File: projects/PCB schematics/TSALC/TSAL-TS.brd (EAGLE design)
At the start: 81.3 x 95.2 mm, 29 parts, among them J1 2P_1-770166-0, J2 2P_1-770166-0, J3 2P_1-770166-0, J4 2P_1-770166-0, X2 5566-2, X3 5566-2

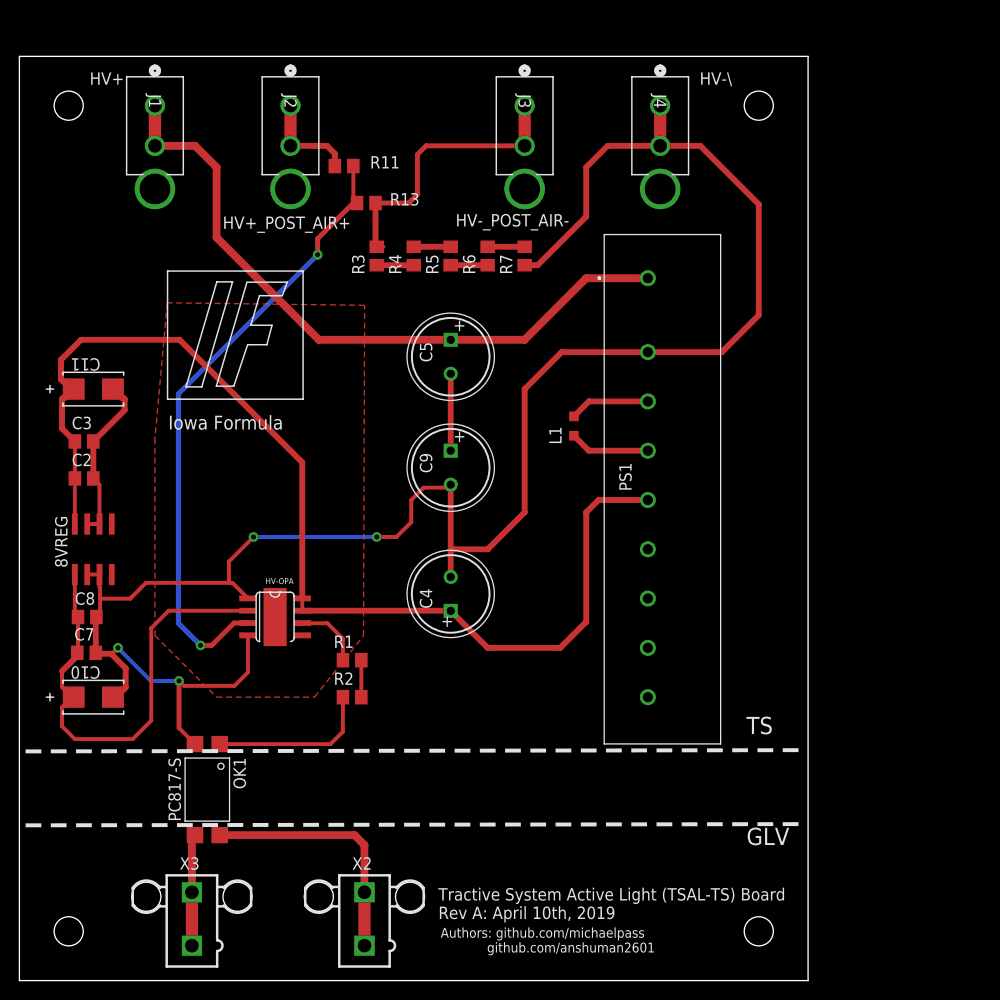
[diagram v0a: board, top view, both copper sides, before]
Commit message: TSALC - TS; Rev A.
Adding in silkscreen markings.
Board has TS and GLV markings separated by 8.26mm. This is the limit imposed by the optocoupler. The rules state that optocouplers are exempt. However, they will likely consider any copper leading up to the device to be TS components to be dealt with.

TSALC - TS; Rev A. Pull request #5.

TSALC boards now ready for pull request review.

---SQUASH---

TSALC - Capacitors updated with new EDA files.

Capacitors now current.
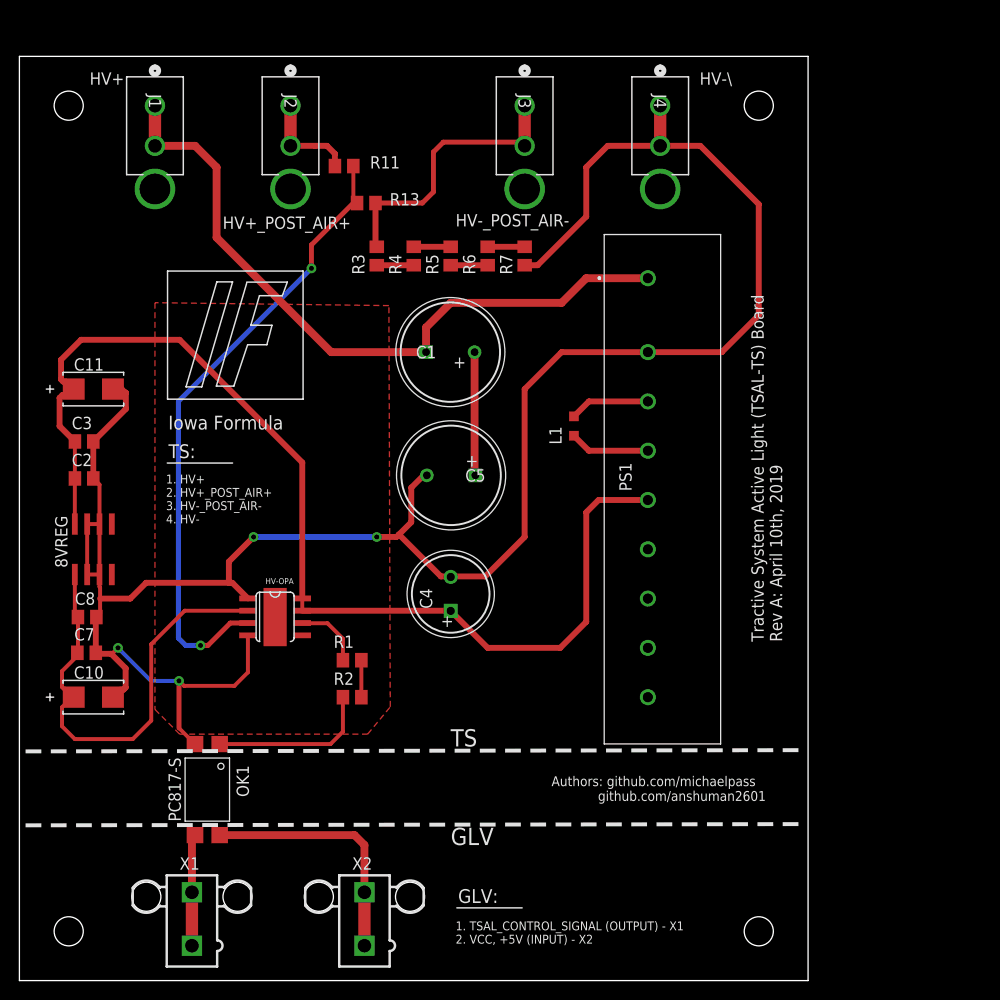
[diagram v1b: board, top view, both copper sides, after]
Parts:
- removed C9: EEU-FS1H221L, EEU-FS1H221L:CAPPRD350W65D800H2200
- added C1: EKXF451ELL100MJ20S, EKXF451ELL100MJ20S:CAPPRD500W60D1025H2150
- C5: value EEU-FS1H221L -> EKXF451ELL100MJ20S; device EEU-FS1H221L:CAPPRD350W65D800H2200 -> EKXF451ELL100MJ20S:CAPPRD500W60D1025H2150
- moved C5 14.2 mm to (47.0, 52.1), turned to 180 degrees
- renumbered X3 to X1
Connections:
- net HV+: now also C1.1; no longer C5.1
- net HV-: now also C5.2; no longer C9.2
- net N$3: now also C1.2, C5.1; no longer C5.2, C9.1
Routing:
- net HV-: track 217.0 -> 227.1 mm
- net N$3: track 7.93 -> 12.7 mm
- net HV+: track 70.1 -> 72.6 mm
- net +8V: track 48.7 -> 47.5 mm
- net SIGNAL_VDIV: track 64.2 -> 65.1 mm
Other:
- board text added: "1. HV+ 2. HV+_POST_AIR+ 3. HV-_POST_AIR- 4. HV-"
- board text added: "1. TSAL_CONTROL_SIGNAL (OUTPUT) - X1 2. VCC, +5V (INPUT) - X2"
- board text added: "GLV:"
- board text added: "TS:"

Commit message: TSAL - Minor fixes.
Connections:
- net HV+_POST_AIR+ renamed MOTORCONTROLLER+
- net HV-_POST_AIR- renamed MOTORCONTROLLER-
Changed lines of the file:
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@@
 <wire x1="33.34" y1="35.24" x2="33.34" y2="33.02" width="0.4064" layer="1"/>
-</signal>
-<signal name="HV+_POST_AIR+">
-<contactref element="R11" pad="2"/>
-<contactref element="J2" pad="1"/>
-<contactref element="J2" pad="2"/>
-<wire x1="27.94" y1="90.17" x2="27.94" y2="86.0298" width="1.27" layer="1"/>
-<wire x1="27.94" y1="86.0298" x2="30.4317" y2="86.0298" width="0.6096" layer="1"/>
-<wire x1="30.4317" y1="86.0298" x2="31.6992" y2="86.0298" width="0.6096" layer="1"/>
-<wire x1="32.5145" y1="85.2145" x2="32.5145" y2="83.947" width="0.6096" layer="1"/>
-<wire x1="31.6992" y1="86.0298" x2="32.5145" y2="85.2145" width="0.6096" layer="1"/>
 </signal>
 <signal name="TSAL_CONTROL_SIGNAL">
@@
 <wire x1="29.1525" y1="53.3975" x2="16.51" y2="66.04" width="0.6096" layer="1"/>
 </signal>
-<signal name="HV-_POST_AIR-">
-<contactref element="J3" pad="1"/>
-<contactref element="J3" pad="2"/>
-<contactref element="R13" pad="1"/>
-<contactref element="R3" pad="1"/>
-<wire x1="52.07" y1="90.17" x2="52.07" y2="86.0298" width="1.27" layer="1"/>
-<wire x1="52.07" y1="86.0298" x2="51.689" y2="86.4108" width="0.508" layer="1"/>
-<wire x1="51.689" y1="86.4108" x2="43.688" y2="86.4108" width="0.508" layer="1"/>
-<wire x1="41.529" y1="80.137" x2="42.672" y2="81.28" width="0.508" layer="1"/>
-<wire x1="42.672" y1="85.3948" x2="43.688" y2="86.4108" width="0.508" layer="1"/>
-<wire x1="36.7005" y1="80.137" x2="41.529" y2="80.137" width="0.508" layer="1"/>
-<wire x1="42.672" y1="81.28" x2="42.672" y2="85.3948" width="0.508" layer="1"/>
-<wire x1="36.83" y1="75.626" x2="36.7005" y2="75.7555" width="0.8128" layer="1"/>
-<wire x1="36.7005" y1="75.7555" x2="36.7005" y2="80.137" width="0.6096" layer="1"/>
-</signal>
 <signal name="N$5">
 <contactref element="R3" pad="2"/>
@@
 <wire x1="46.91" y1="52.15" x2="46.99" y2="52.07" width="0.8128" layer="1"/>
 </signal>
+<signal name="MOTORCONTROLLER+">
+<contactref element="J2" pad="1"/>
+<contactref element="J2" pad="2"/>
+<wire x1="27.94" y1="90.17" x2="27.94" y2="86.0298" width="1.27" layer="1"/>
+<contactref element="R11" pad="2"/>
+<wire x1="32.5145" y1="85.2145" x2="32.5145" y2="83.947" width="0.6096" layer="1"/>
+<wire x1="31.6992" y1="86.0298" x2="32.5145" y2="85.2145" width="0.6096" layer="1"/>
+<wire x1="27.94" y1="86.0298" x2="31.6992" y2="86.0298" width="0.6096" layer="1"/>
+</signal>
+<signal name="MOTORCONTROLLER-">
+<contactref element="J3" pad="1"/>
+<contactref element="J3" pad="2"/>
+<contactref element="R13" pad="1"/>
+<contactref element="R3" pad="1"/>
+<wire x1="41.529" y1="80.137" x2="42.672" y2="81.28" width="0.508" layer="1"/>
+<wire x1="36.7005" y1="80.137" x2="41.529" y2="80.137" width="0.508" layer="1"/>
+<wire x1="42.672" y1="81.28" x2="42.672" y2="85.09" width="0.508" layer="1"/>
+<wire x1="36.83" y1="75.626" x2="36.7005" y2="75.7555" width="0.8128" layer="1"/>
+<wire x1="36.7005" y1="75.7555" x2="36.7005" y2="80.137" width="0.6096" layer="1"/>
+<wire x1="52.07" y1="90.17" x2="52.07" y2="86.0298" width="1.27" layer="1"/>
+<wire x1="42.672" y1="85.09" x2="43.6118" y2="86.0298" width="0.508" layer="1"/>
+<wire x1="43.6118" y1="86.0298" x2="52.07" y2="86.0298" width="0.508" layer="1"/>
+</signal>
 </signals>

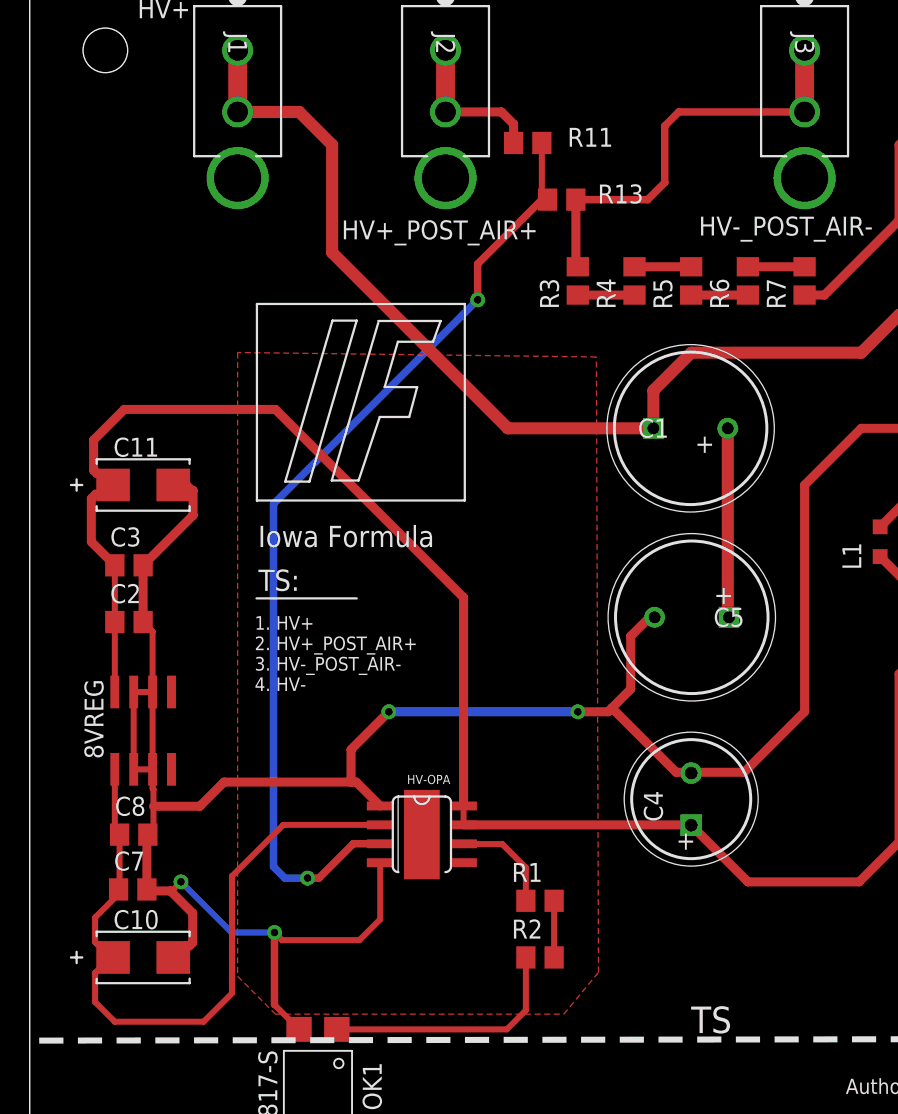
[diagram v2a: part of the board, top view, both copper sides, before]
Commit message: TSAL - Added in FUSE to HV sense line.
Added in FUSE and removed redundant tantalum capacitors.
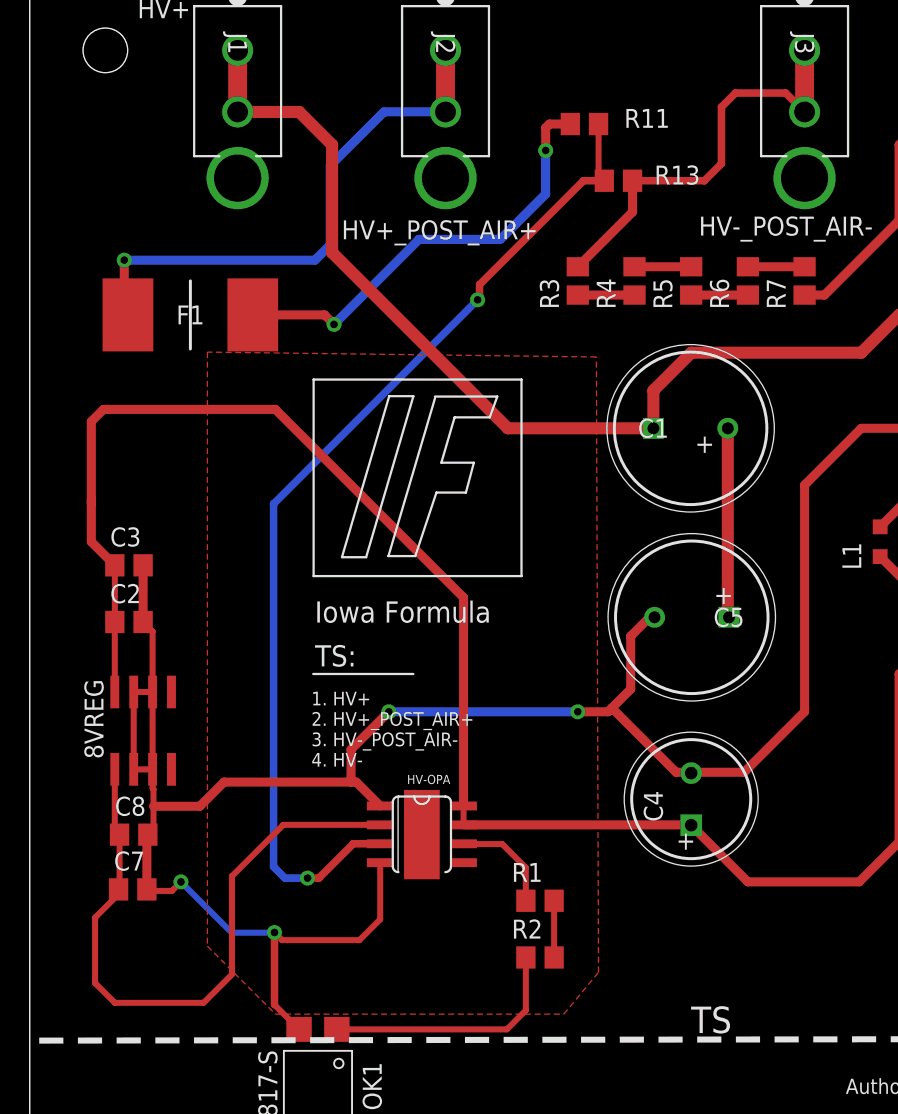
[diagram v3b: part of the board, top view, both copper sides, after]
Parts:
- removed C10, C11: T491C106K020AT, T491C106K020AT:CAPT6032N
- added F1: 0885001.DR, 0885001.DR:FUSC10948X488N
- moved R11 4.02 mm to (37.3, 85.2)
- moved R13 4.02 mm to (39.6, 81.4)
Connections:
- new net MOTORCONTROLLER+_POST_FUSE: F1.2, R11.2
- net +15V-NONISO: no longer C11.1
- net +8V: no longer C10.1
- net HV-: no longer C10.2, C11.2
- net MOTORCONTROLLER+: now also F1.1; no longer R11.2
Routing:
- net MOTORCONTROLLER+_POST_FUSE: track 0.00 -> 29.8 mm, vias 0 -> 2
- net MOTORCONTROLLER+: track 10.3 -> 36.8 mm, vias 0 -> 1
- net HV-: track 227.1 -> 213.4 mm
- net +8V: track 47.5 -> 43.7 mm
- net SIGNAL_VDIV: track 65.1 -> 68.6 mm
- net MOTORCONTROLLER-: track 28.7 -> 28.2 mm

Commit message: TSAL - Resizing.
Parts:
- moved PS1 15.2 mm to (80.0, 72.4)
- moved L1 15.2 mm to (72.4, 57.1)
- moved X1 12.8 mm to (30.5, 7.62), turned to 180 degrees
- moved X2 11.5 mm to (47.0, 7.62), turned to 180 degrees
- moved C1 10.2 mm to (52.1, 64.8)
- moved HV-OPA 10.2 mm to (36.5, 37.5)
- moved R1 10.2 mm to (44.5, 33.0)
- moved R13 10.2 mm to (49.7, 81.4)
- moved R2 10.2 mm to (44.5, 29.2)
- moved R3 10.2 mm to (47.0, 74.7)
- moved R6 10.2 mm to (58.4, 74.7)
- moved 8VREG 10.2 mm to (17.8, 44.5)
- moved C2 10.2 mm to (16.8, 51.8)
- moved C3 10.2 mm to (16.8, 55.6)
- moved C8 10.2 mm to (17.1, 37.5)
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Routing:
- net HV-: track 213.4 -> 220.6 mm
- net HV+: track 72.6 -> 77.7 mm
- net +15V-NONISO: track 115.2 -> 116.9 mm
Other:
- board size 81.3 x 95.2 mm -> 99.1 x 99.1 mm
- board text added: "MOTORCONTROLLER+"
- board text added: "MOTORCONTROLLER-"
- board text removed: "HV+_POST_AIR+"
- board text removed: "HV-_POST_AIR-"

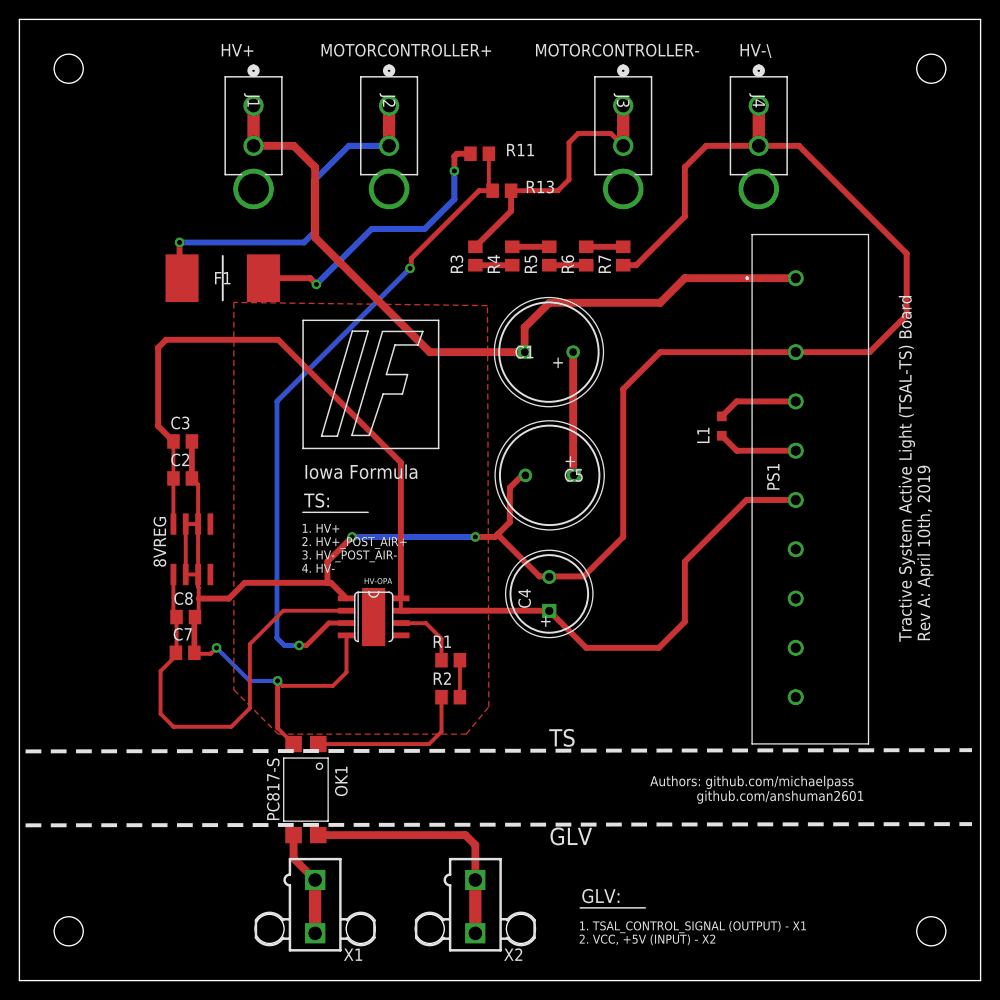
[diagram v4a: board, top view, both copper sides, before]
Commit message: TSAL - Added in fuses.
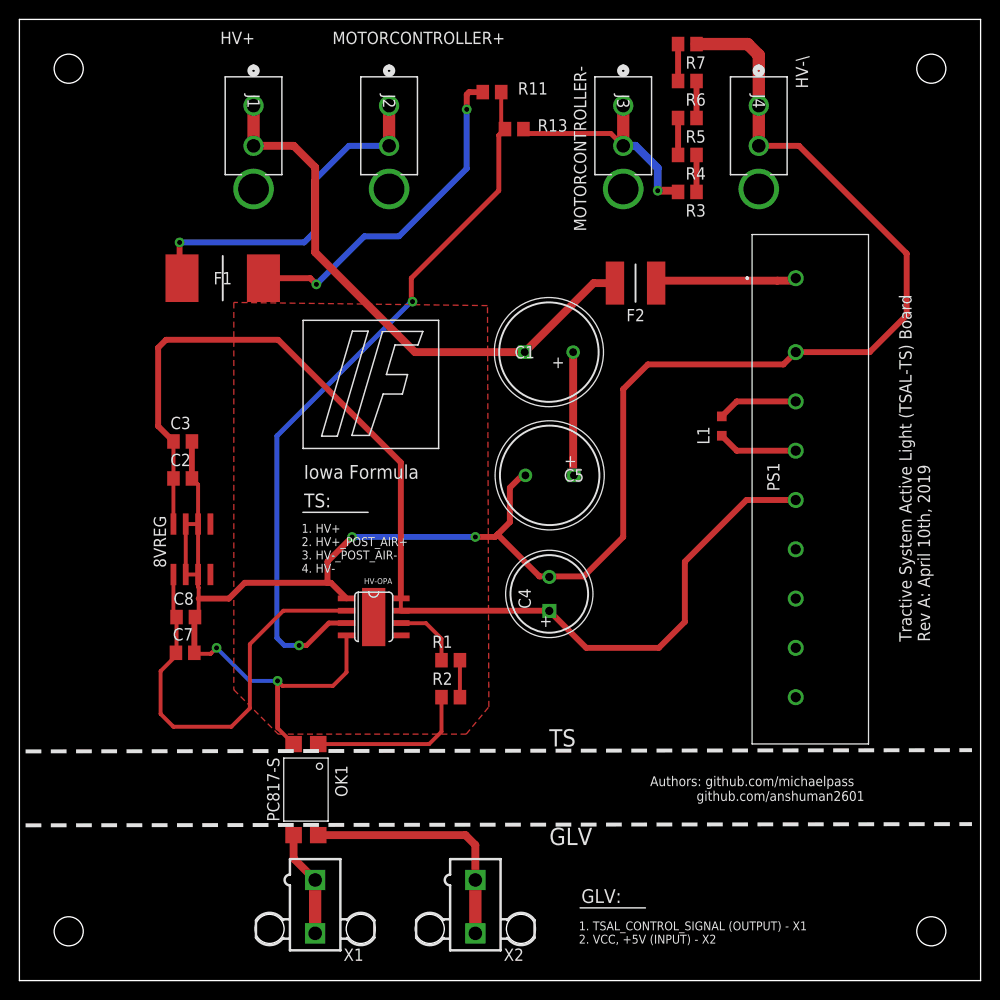
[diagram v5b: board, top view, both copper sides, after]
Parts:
- added F2: 2016L030DR, SamacSys_Parts:FUSC5141X125N
- moved R3 22.8 mm to (68.8, 81.3), turned to 0 degrees
- moved R7 22.8 mm to (68.8, 96.5), turned to 0 degrees
- moved R4 20.8 mm to (68.8, 85.1), turned to 180 degrees
- moved R6 20.8 mm to (68.8, 92.7), turned to 180 degrees
- moved R5 20.1 mm to (68.8, 88.9), turned to 0 degrees
- moved R13 6.48 mm to (51.0, 87.8)
- moved R11 6.48 mm to (48.7, 91.6)
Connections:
- new net N$4: F2.2, PS1.1
- net HV+: now also F2.1; no longer PS1.1
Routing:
- net HV+: track 77.7 -> 58.3 mm
- net N$4: track 0.00 -> 14.6 mm
- net HV-: track 220.6 -> 211.0 mm
- net SIGNAL_VDIV: track 68.6 -> 75.0 mm
- net MOTORCONTROLLER+_POST_FUSE: track 29.8 -> 35.5 mm
- net MOTORCONTROLLER-: track 28.2 -> 24.2 mm, vias 0 -> 1
